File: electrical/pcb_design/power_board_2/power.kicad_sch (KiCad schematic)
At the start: 11 parts, among them U8 TPS63900

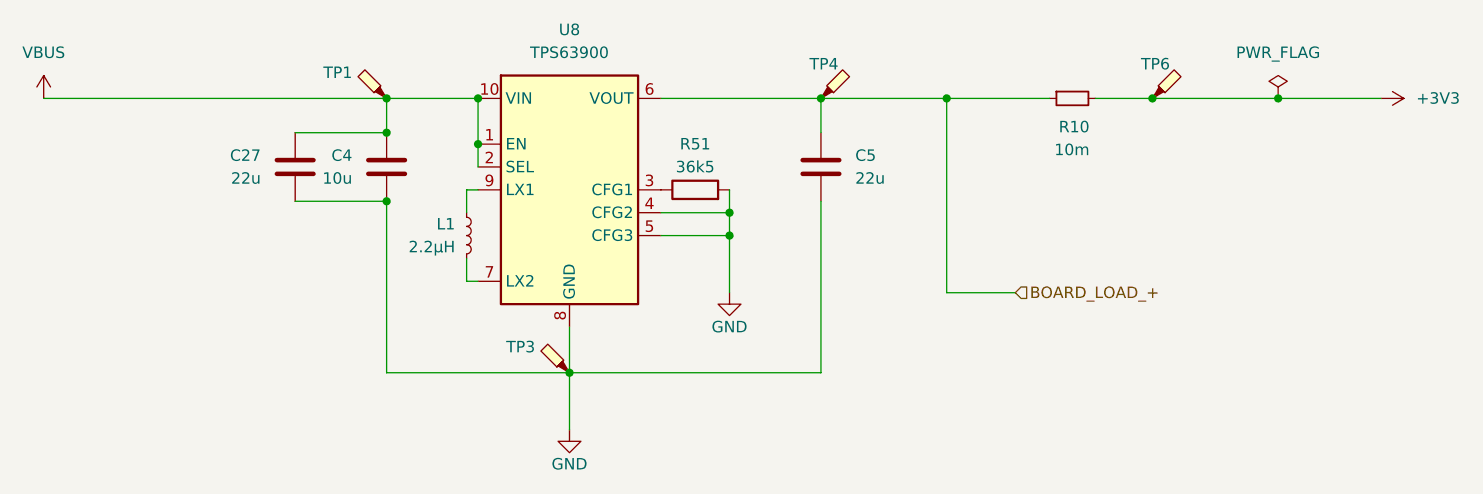
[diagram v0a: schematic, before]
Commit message: power board schematic complete except board id
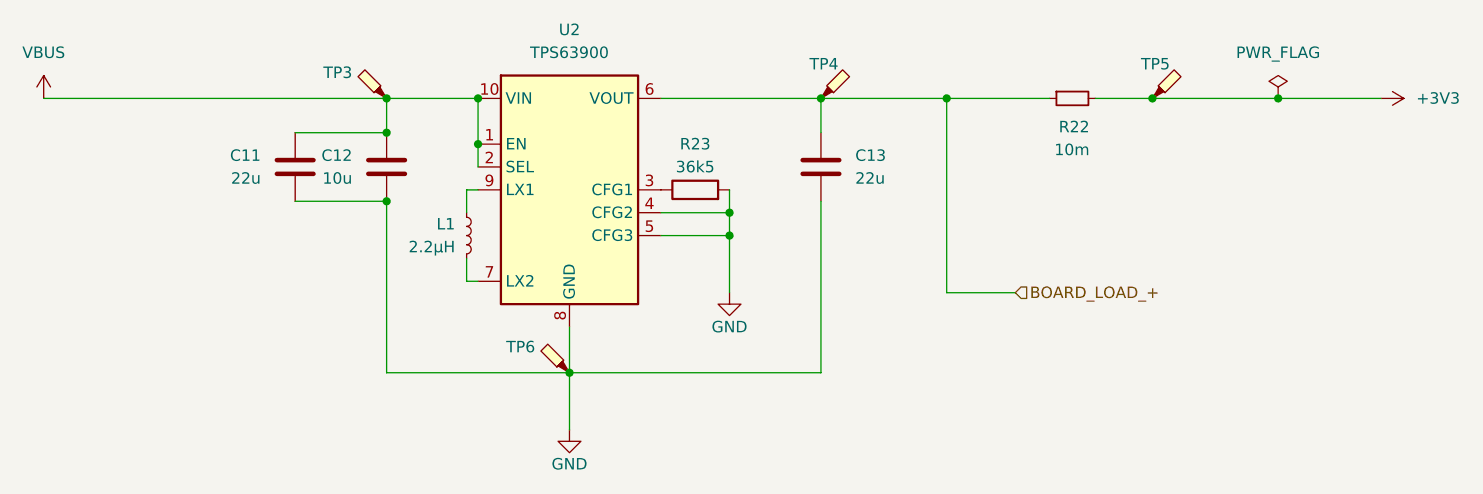
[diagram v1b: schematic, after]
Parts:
- renumbered C27 to C11, C4 to C12, C5 to C13, R10 to R22, R51 to R23, TP1 to TP3, TP6 to TP5, TP3 to TP6, U8 to U2
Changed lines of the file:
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@@
 		(on_board yes)
 		(dnp no)
-		(property "Reference" "U8"
+		(property "Reference" "U2"
 			(at 132.08 69.85 0)
 			(effects
@@
 			(project ""
 				(path "/695f882b-5312-4493-b26d-8f7d6768a9db/7f8fc7f5-7f1e-476b-9e93-5575de1d6778"
-					(reference "U8")
+					(reference "U2")
 					(unit 1)
 				)
@@
 		(on_board yes)
 		(dnp no)
-		(property "Reference" "R51"
+		(property "Reference" "R23"
 			(at 146.05 82.55 90)
 			(effects
@@
 			(project "1s3p_battery_board"
 				(path "/695f882b-5312-4493-b26d-8f7d6768a9db/7f8fc7f5-7f1e-476b-9e93-5575de1d6778"
-					(reference "R51")
+					(reference "R23")
 					(unit 1)
 				)
@@
 		(on_board yes)
 		(dnp no)
-		(property "Reference" "TP1"
+		(property "Reference" "TP3"
 			(at 107.95 74.6125 0)
 			(effects
@@
 			(project "1s3p_battery_board"
 				(path "/695f882b-5312-4493-b26d-8f7d6768a9db/7f8fc7f5-7f1e-476b-9e93-5575de1d6778"
-					(reference "TP1")
+					(reference "TP3")
 					(unit 1)
 				)
@@
 		(on_board yes)
 		(dnp no)
-		(property "Reference" "#PWR23"
+		(property "Reference" "#PWR026"
 			(at 218.44 77.47 0)
 			(effects
@@
 			(project "1s3p_battery_board"
 				(path "/695f882b-5312-4493-b26d-8f7d6768a9db/7f8fc7f5-7f1e-476b-9e93-5575de1d6778"
-					(reference "#PWR23")
+					(reference "#PWR026")
 					(unit 1)
 				)
@@
 		(on_board yes)
 		(dnp no)
-		(property "Reference" "TP6"
+		(property "Reference" "TP5"
 			(at 195.58 73.66 0)
 			(effects
@@
 			(project "1s3p_battery_board"
 				(path "/695f882b-5312-4493-b26d-8f7d6768a9db/7f8fc7f5-7f1e-476b-9e93-5575de1d6778"
-					(reference "TP6")
+					(reference "TP5")
 					(unit 1)
 				)
@@
 		(on_board yes)
 		(dnp no)
-		(property "Reference" "R10"
+		(property "Reference" "R22"
 			(at 189.865 80.6449 90)
 			(effects
@@
 			(project "1s3p_battery_board"
 				(path "/695f882b-5312-4493-b26d-8f7d6768a9db/7f8fc7f5-7f1e-476b-9e93-5575de1d6778"
-					(reference "R10")
+					(reference "R22")
 					(unit 1)
 				)
@@
 		(on_board yes)
 		(dnp no)
-		(property "Reference" "TP3"
+		(property "Reference" "TP6"
 			(at 128.27 105.0925 0)
 			(effects
@@
 			(project "1s3p_battery_board"
 				(path "/695f882b-5312-4493-b26d-8f7d6768a9db/7f8fc7f5-7f1e-476b-9e93-5575de1d6778"
-					(reference "TP3")
+					(reference "TP6")
 					(unit 1)
 				)
@@
 		(on_board yes)
 		(dnp no)
-		(property "Reference" "#PWR88"
+		(property "Reference" "#PWR028"
 			(at 132.08 120.65 0)
 			(effects
@@
 			(project "1s3p_battery_board"
 				(path "/695f882b-5312-4493-b26d-8f7d6768a9db/7f8fc7f5-7f1e-476b-9e93-5575de1d6778"
-					(reference "#PWR88")
+					(reference "#PWR028")
 					(unit 1)
 				)
@@
 		(dnp no)
 		(fields_autoplaced yes)
-		(property "Reference" "#PWR14"
+		(property "Reference" "#PWR025"
 			(at 73.66 81.28 0)
 			(effects
@@
 			(project "1s3p_battery_board"
 				(path "/695f882b-5312-4493-b26d-8f7d6768a9db/7f8fc7f5-7f1e-476b-9e93-5575de1d6778"
-					(reference "#PWR14")
+					(reference "#PWR025")
 					(unit 1)
 				)
@@
 		(dnp no)
 		(fields_autoplaced yes)
-		(property "Reference" "#FLG3"
+		(property "Reference" "#FLG01"
 			(at 210.82 75.565 0)
 			(effects
@@
 			(project "1s3p_battery_board"
 				(path "/695f882b-5312-4493-b26d-8f7d6768a9db/7f8fc7f5-7f1e-476b-9e93-5575de1d6778"
-					(reference "#FLG3")
+					(reference "#FLG01")
 					(unit 1)
 				)
@@
 		(on_board yes)
 		(dnp no)
-		(property "Reference" "C27"
+		(property "Reference" "C11"
 			(at 97.79 83.82 0)
 			(effects
@@
 			(project "1s3p_battery_board"
 				(path "/695f882b-5312-4493-b26d-8f7d6768a9db/7f8fc7f5-7f1e-476b-9e93-5575de1d6778"
-					(reference "C27")
+					(reference "C11")
 					(unit 1)
 				)
@@
 		(on_board yes)
 		(dnp no)
-		(property "Reference" "C4"
+		(property "Reference" "C12"
 			(at 107.95 83.82 0)
 			(effects
@@
 			(project "1s3p_battery_board"
 				(path "/695f882b-5312-4493-b26d-8f7d6768a9db/7f8fc7f5-7f1e-476b-9e93-5575de1d6778"
-					(reference "C4")
+					(reference "C12")
 					(unit 1)
 				)
@@
 		(on_board yes)
 		(dnp no)
-		(property "Reference" "#PWR89"
+		(property "Reference" "#PWR027"
 			(at 149.86 105.41 0)
 			(effects
@@
 			(project "1s3p_battery_board"
 				(path "/695f882b-5312-4493-b26d-8f7d6768a9db/7f8fc7f5-7f1e-476b-9e93-5575de1d6778"
-					(reference "#PWR89")
+					(reference "#PWR027")
 					(unit 1)
 				)
@@
 		(dnp no)
 		(fields_autoplaced yes)
-		(property "Reference" "C5"
+		(property "Reference" "C13"
 			(at 163.83 83.82 0)
 			(effects
@@
 			(project "1s3p_battery_board"
 				(path "/695f882b-5312-4493-b26d-8f7d6768a9db/7f8fc7f5-7f1e-476b-9e93-5575de1d6778"
-					(reference "C5")
+					(reference "C13")
 					(unit 1)
 				)

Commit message: begin schematic review edits
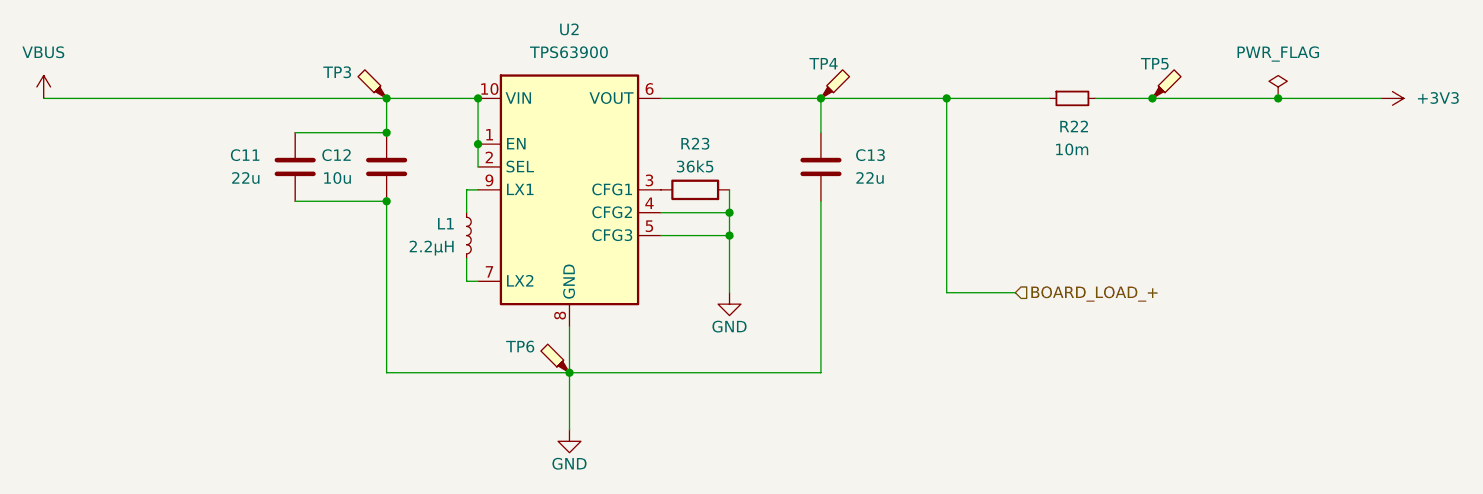
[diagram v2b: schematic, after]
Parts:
- C11, C13: footprint footprints:Nondescript_C_0603_1608Metric -> (none); Active Y -> (none); Basic or Extended Component Extended -> (none); MPN C710887 -> (none); Manufacturer Murata -> (none); Manufacturer Part Number GRM187R60J226ME15D -> (none); Purpose Voltage regulator -> (none)
- C12: footprint footprints:Nondescript_C_0603_1608Metric -> (none); Active Y -> (none); Basic or Extended Component Extended -> (none); MPN C77041 -> (none); Manufacturer Murata -> (none); Manufacturer Part Number GRM188R60J106ME47D -> (none); Purpose Voltage regulator -> (none); Specs 3.3V -> (none)
- L1: footprint Inductor_SMD:L_1008_2520Metric -> (none); Active Y -> (none); Basic or Extended Component Extended -> (none); MPN C576403 -> (none); Manufacturer Murata -> (none); Manufacturer Part Number DFE252012F-2R2M=P2 -> (none)
- R22: footprint Resistor_SMD:R_2512_6332Metric -> (none); Active Y -> (none); Basic or Extended Component Extended -> (none); MPN C241862 -> (none); Manufacturer Vishay Intertech -> (none); Manufacturer Part Number WSLP2512R0100FEA -> (none)
- R23: footprint footprints:Nondescript_R_0603_1608Metric -> (none); Active Y -> (none); Basic or Extended Component Extended -> (none); MPN C23029 -> (none); Manufacturer UNI-ROYAL(Uniroyal Elec) -> (none); Manufacturer Part Number 0603WAF3652T5E -> (none)
- TP3, TP4, TP5, TP6: footprint footprints:TestPoint_Pad_D1.5mm -> (none); Active Y -> (none); MPN NA -> (none); now in the parts list
- U2: footprint Package_SON:WSON-10-1EP_2.5x2.5mm_P0.5mm_EP1.2x2mm -> Package_SON:WSON-10-1EP_2.5x2.5mm_P0.5mm_EP1.2x2mm_ThermalVias; Active Y -> (none); Basic or Extended Component Extended -> (none); MPN C1518762 -> (none); Manufacturer Texas Instruments -> (none); Manufacturer Part Number TPS63900DSKR -> (none)

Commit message: begin footprint assignment
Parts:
- C11, C12, C13: footprint (none) -> footprints:Nondescript_C_0402_1005Metric
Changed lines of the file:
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@@
 			)
 		)
-		(property "Footprint" ""
+		(property "Footprint" "footprints:Nondescript_C_0402_1005Metric"
 			(at 100.6348 88.9 0)
 			(effects
@@
 			)
 		)
-		(property "Footprint" ""
+		(property "Footprint" "footprints:Nondescript_C_0402_1005Metric"
 			(at 110.7948 88.9 0)
 			(effects
@@
 			)
 		)
-		(property "Footprint" ""
+		(property "Footprint" "footprints:Nondescript_C_0402_1005Metric"
 			(at 160.9852 88.9 0)
 			(effects

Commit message: footprint selection
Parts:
- TP3, TP4, TP5, TP6: footprint (none) -> footprints:TestPoint_Pad_D1.5mm
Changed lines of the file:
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@@
 			)
 		)
-		(property "Footprint" ""
+		(property "Footprint" "footprints:TestPoint_Pad_D1.5mm"
 			(at 106.68 77.47 0)
 			(effects
@@
 			)
 		)
-		(property "Footprint" ""
+		(property "Footprint" "footprints:TestPoint_Pad_D1.5mm"
 			(at 165.1 77.47 0)
 			(effects
@@
 			)
 		)
-		(property "Footprint" ""
+		(property "Footprint" "footprints:TestPoint_Pad_D1.5mm"
 			(at 201.93 77.47 0)
 			(effects
@@
 			)
 		)
-		(property "Footprint" ""
+		(property "Footprint" "footprints:TestPoint_Pad_D1.5mm"
 			(at 127 107.95 0)
 			(effects

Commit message: reristor selection
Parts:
- L1: footprint (none) -> Inductor_SMD:L_1008_2520Metric
- R23: footprint (none) -> footprints:Nondescript_R_0603_1608Metric
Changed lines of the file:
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@@
 			)
 		)
-		(property "Footprint" ""
+		(property "Footprint" "Inductor_SMD:L_1008_2520Metric"
 			(at 120.65 92.71 0)
 			(effects
@@
 			)
 		)
-		(property "Footprint" ""
+		(property "Footprint" "footprints:Nondescript_R_0603_1608Metric"
 			(at 146.05 89.408 90)
 			(effects

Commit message: finish initial component selection and start layout
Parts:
- R22: footprint (none) -> Resistor_SMD:R_2512_6332Metric
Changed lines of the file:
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@@
 			)
 		)
-		(property "Footprint" ""
+		(property "Footprint" "Resistor_SMD:R_2512_6332Metric"
 			(at 187.96 77.47 0)
 			(effects

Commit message: mcu placement
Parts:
- removed TP3: VBUS, footprints:TestPoint_Pad_D1.5mm, symbol Connector:TestPoint_Probe
- removed TP4: BOARD_LOAD_+, footprints:TestPoint_Pad_D1.5mm, symbol Connector:TestPoint_Probe
- removed TP5: +3V3, footprints:TestPoint_Pad_D1.5mm, symbol Connector:TestPoint_Probe
- removed TP6: GND, footprints:TestPoint_Pad_D1.5mm, symbol Connector:TestPoint_Probe
